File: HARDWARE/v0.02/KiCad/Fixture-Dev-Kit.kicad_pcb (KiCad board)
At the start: 2 copper layers, 151 x 130.6 mm, 182 parts, among them J1 DUT, J10 LED_3, J11 FET_0, J12 FET_0, J13 NFET_0, J14 NFET_1, J15 Conn_01x20, J16 Conn_01x20, J17 CHIP4RH, J18 SW_0, J19 SW_0, J2 POWER, J20 Conn_01x20, J21 Conn_01x20, J22 SW_0, J23 CHIP4LH, J24 SW_0, J25 JST-2P-RA, J26 SW_0, J27 INA_40, J28 INA_40, J29 INA_40, J3 LED_0, J30 INA_40, J31 ADS, J32 SW_0, J33 SW_0, J34 SW_0, J35 40 V+, J36 41 V+, J37 42 V+, J38 43 V+, J39 DUT BAT, J4 LED_1, J40 DUT BAT, J41 Conn_01x05, J5 LED_2, J6 LED_3, J7 LED_0, J8 LED_1, J9 LED_2, Q1 NTF2955T1G, Q10 NTF2955-D, Q11 NTF2955-D, Q12 NTF2955-D, Q13 FDN337N, Q14 FDN337N, Q15 FDN337N, Q16 FDN337N, Q2 NTF2955T1G, Q3 FDN337N, Q4 FDN337N, Q5 NTF2955-D, Q6 NTF2955-D, Q7 NTF2955-D, Q8 NTF2955-D, Q9 NTF2955-D, SW1 TL9210AF260Q, SW2 TL9210AF260Q, SW3 TL9210AF260Q, SW4 TL9210AF260Q, SW5 YSS-19-1202-N, SW6 TL9210AF260Q, U1 INA219BIDCNT, U2 INA219BIDCNT, U3 INA219BIDCNT, U4 INA219BIDCNT, U5 ADS1015IDGST

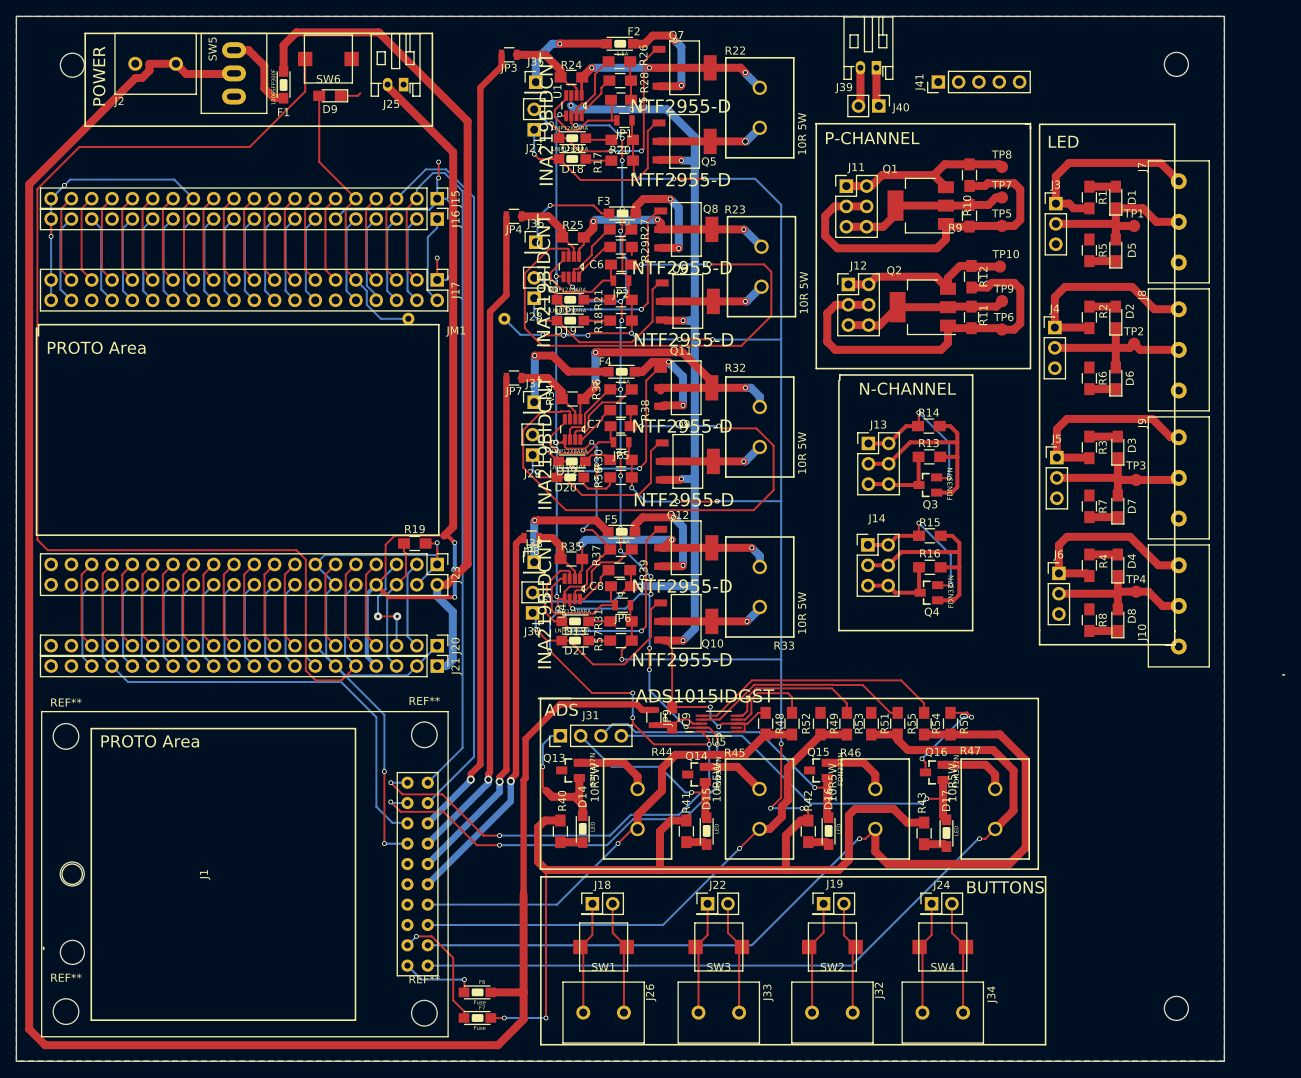
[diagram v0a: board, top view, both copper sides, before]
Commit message: updating C4 Functional computer footprint, creating compressed folder
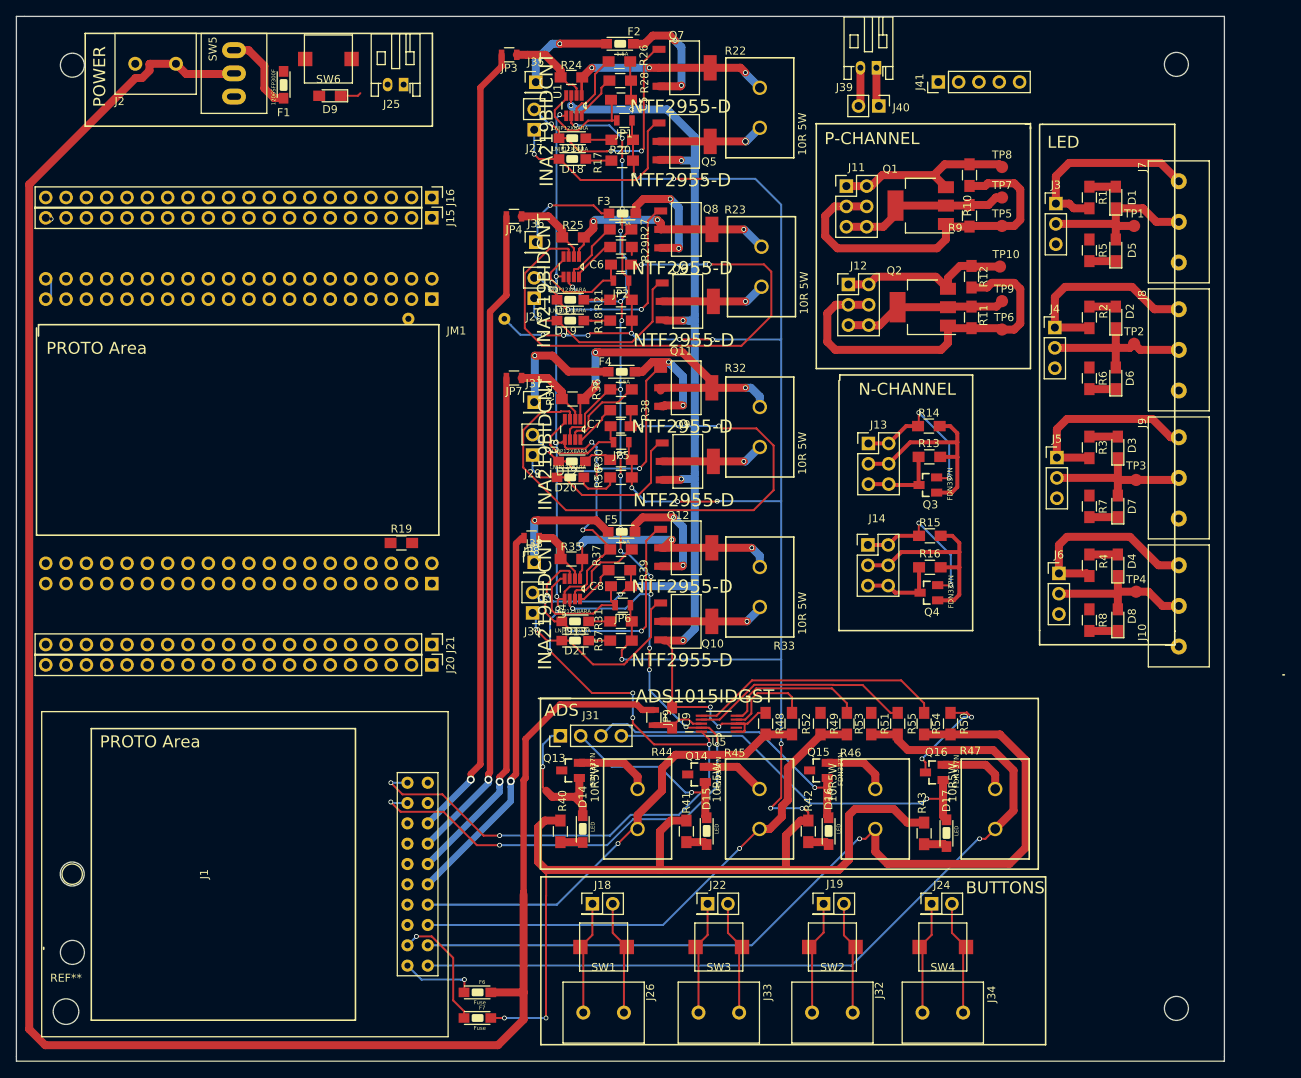
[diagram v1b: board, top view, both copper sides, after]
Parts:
- removed the REF** at (29.2, 108.0)
- removed the REF** at (74.0, 142.6)
- removed the REF** at (74.0, 107.8)
- J17, J23: moved to B.Cu
- moved J21 2.77 mm to (74.9, 96.5)
- moved J16 2.77 mm to (74.9, 40.6)
- moved J17 2.49 mm to (74.9, 53.3), turned to 90 degrees
- moved J20 2.49 mm to (74.9, 99.1)
- moved J23 2.49 mm to (74.9, 88.9), turned to 90 degrees
- moved J15 2.49 mm to (74.9, 43.2)
- moved R19 1.68 mm to (71.1, 83.8)
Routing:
- net GND: track 488.9 -> 323.6 mm, vias 26 -> 18
- net /Fixture Dev Kit - Functional Computer/PWRON: track 153.7 -> 0.00 mm
- net /Fixture Dev Kit - Functional Computer/C4-PWR-IN: track 104.2 -> 0.00 mm
- net /Fixture Dev Kit - Functional Computer/BAT: track 103.6 -> 0.25 mm, vias 2 -> 0
- net /UART-RX: track 102.2 -> 0.00 mm
- net /UART-TX: track 95.9 -> 0.00 mm
- net /ADAPTER_ID: track 63.1 -> 0.10 mm
- net /Fixture Dev Kit - Functional Computer/STATUSLED: track 35.6 -> 0.00 mm
- net /Fixture Dev Kit - Functional Computer/TS: track 16.9 -> 0.00 mm
- net Net-(J20-Pad3): track 13.8 -> 0.00 mm, vias 2 -> 0
- net Net-(J20-Pad2): track 11.4 -> 0.00 mm
- net Net-(J21-Pad15): track 11.3 -> 0.00 mm
- net Net-(J21-Pad13): track 11.3 -> 0.00 mm
- net Net-(J21-Pad12): track 11.3 -> 0.00 mm
- net Net-(J16-Pad19): track 11.3 -> 0.00 mm
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- removed copper zone on B.Cu, net +5V
- removed copper zone on F.Cu, net GND
